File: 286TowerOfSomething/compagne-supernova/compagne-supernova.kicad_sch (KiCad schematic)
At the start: 3 parts, among them J1 Bus_ISA_16bit, U1 16550, U2 16550

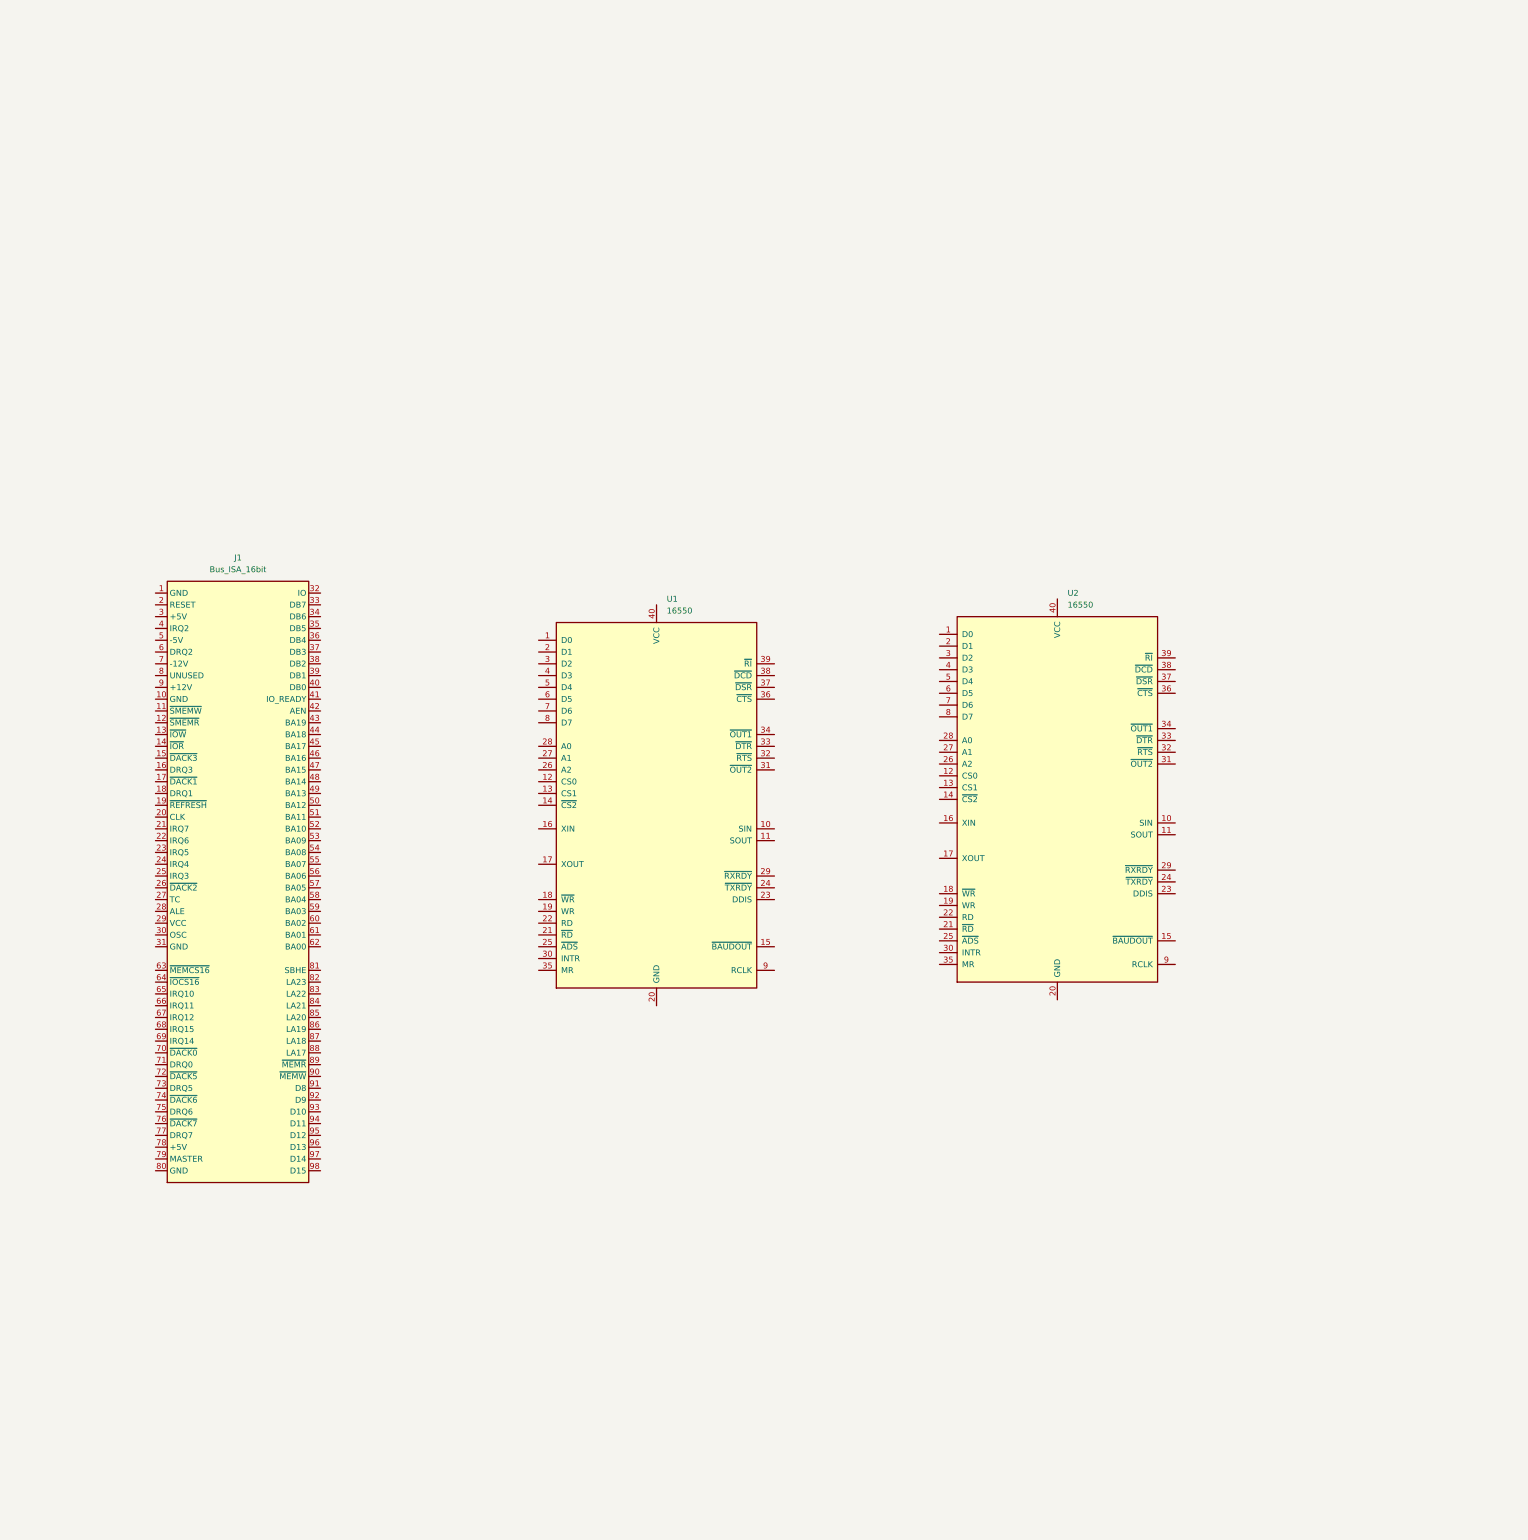
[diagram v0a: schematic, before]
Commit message: Schematic for compagne-supernova at like 50%
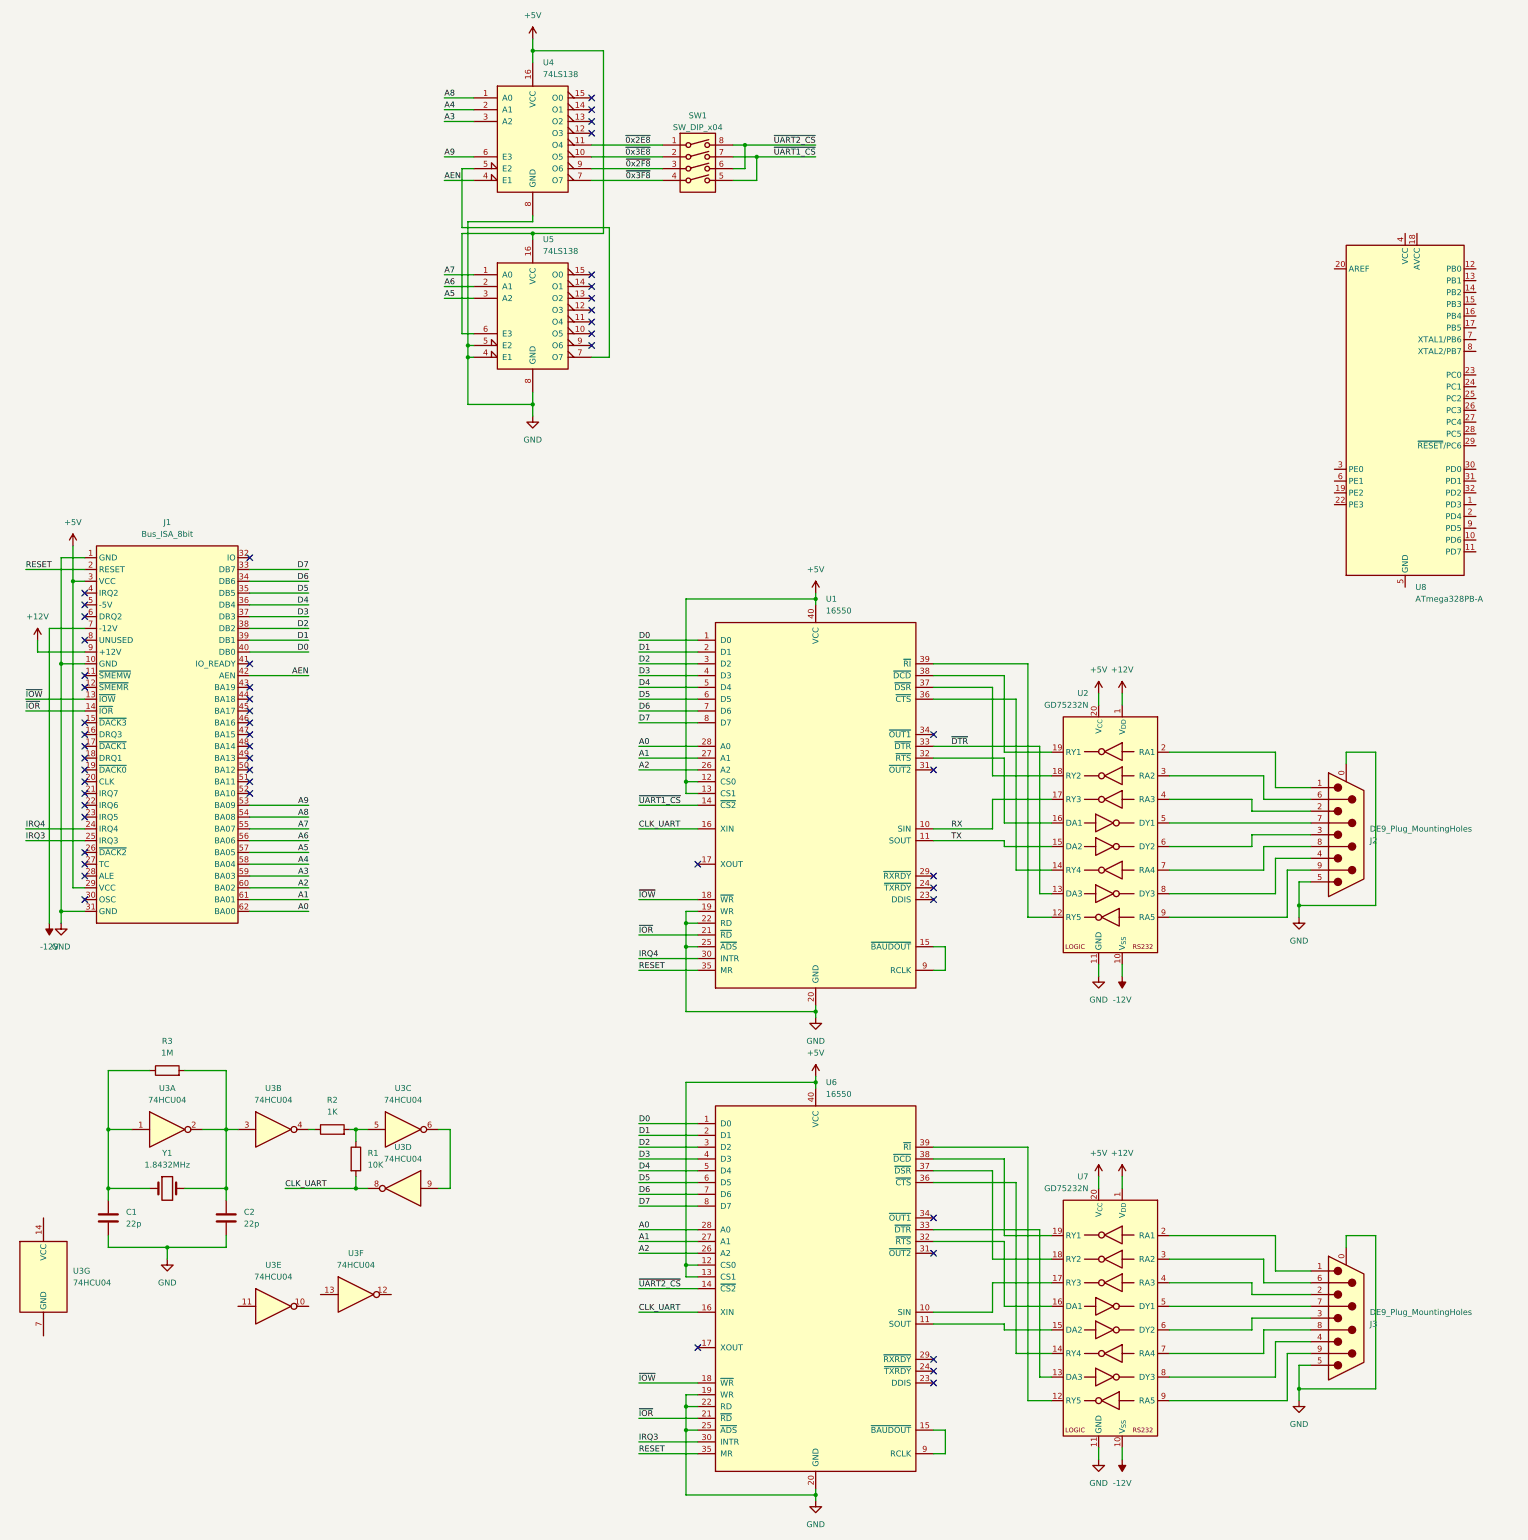
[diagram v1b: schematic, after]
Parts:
- removed J1: Bus_ISA_16bit, symbol Connector:Bus_ISA_16bit
- removed U2: 16550, Package_DIP:DIP-40_W15.24mm, symbol Interface_UART:16550
- added C1, C2: 22p, symbol Device:C
- added J1: Bus_ISA_8bit, symbol Connector:Bus_ISA_8bit
- added J2, J3: DE9_Plug_MountingHoles, symbol Connector:DE9_Plug_MountingHoles
- added R1: 10K, symbol Device:R
- added R2: 1K, symbol Device:R
- added R3: 1M, symbol Device:R
- added SW1: SW_DIP_x04, symbol Switch:SW_DIP_x04
- added U2, U7: GD75232N, Package_DIP:DIP-20_W7.62mm, symbol Interface_UART:GD75232N
- added U3: 74HCU04, symbol 74xx:74HC04
- added U4, U5: 74LS138, symbol 74xx:74LS138
- added U6: 16550, Package_DIP:DIP-40_W15.24mm, symbol Interface_UART:16550
- added U8: ATmega328PB-A, Package_QFP:TQFP-32_7x7mm_P0.8mm, symbol MCU_Microchip_ATmega:ATmega328PB-A
- added Y1: 1.8432MHz, symbol Device:Crystal
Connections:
- net D0: now reaches U1.1 (D0)
- net D0: now also J1.40 (DB0), U6.1 (D0)
- net RX: now reaches U1.10 (SIN)
- net RX: now also U2.17 (RY3)
- net TX: now reaches U1.11 (SOUT)
- net TX: now also U2.15 (DA2)
- net +5V: now reaches U1.12 (CS0)
- net +5V: now also U1.13 (CS1), U1.40 (VCC), J1.29 (VCC), J1.3 (VCC), U2.20 (V_{CC}), U4.16 (VCC), U5.16 (VCC), U5.6 (E3), U6.12 (CS0), U6.13 (CS1), U6.40 (VCC), U7.20 (V_{CC})
- net ~{UART1_CS}: now reaches U1.14 (~{CS2})
- net ~{UART1_CS}: now also SW1.5, SW1.7
- net at U1.15 (~{BAUDOUT}): now also U1.9 (RCLK)
- net CLK_UART: now reaches U1.16 (XIN)
- net CLK_UART: now also R1.2, U3.8, U6.16 (XIN)
- net ~{IOW}: now reaches U1.18 (~{WR})
- net ~{IOW}: now also J1.13 (~{IOW}), U6.18 (~{WR})
- net GND: now reaches U1.19 (WR)
- net GND: now also U1.20 (GND), U1.22 (RD), U1.25 (~{ADS}), C1.2, C2.2, J1.1 (GND), J1.10 (GND), J1.31 (GND), J2.0 (PAD), J2.5, J3.0 (PAD), J3.5, U2.11 (GND), U4.8 (GND), U5.4 (E1), U5.5 (E2), U5.8 (GND), U6.19 (WR), U6.20 (GND), U6.22 (RD), U6.25 (~{ADS}), U7.11 (GND)
- net D1: now reaches U1.2 (D1)
- net D1: now also J1.39 (DB1), U6.2 (D1)
- net ~{IOR}: now reaches U1.21 (~{RD})
- net ~{IOR}: now also J1.14 (~{IOR}), U6.21 (~{RD})
- net A2: now reaches U1.26 (A2)
- net A2: now also J1.60 (BA02), U6.26 (A2)
- net A1: now reaches U1.27 (A1)
- net A1: now also J1.61 (BA01), U6.27 (A1)
- net A0: now reaches U1.28 (A0)
- net A0: now also J1.62 (BA00), U6.28 (A0)
- net D2: now reaches U1.3 (D2)
- net D2: now also J1.38 (DB2), U6.3 (D2)
- net IRQ4: now reaches U1.30 (INTR)
- net IRQ4: now also J1.24 (IRQ4)
- net at U1.32 (~{RTS}): now also U2.16 (DA1)
- net ~{DTR}: now reaches U1.33 (~{DTR})
- net ~{DTR}: now also U2.13 (DA3)
- net RESET: now reaches U1.35 (MR)
- net RESET: now also J1.2 (RESET), U6.35 (MR)
- net at U1.36 (~{CTS}): now also U2.14 (RY4)
- net at U1.37 (~{DSR}): now also U2.18 (RY2)
- net at U1.38 (~{DCD}): now also U2.19 (RY1)
- net at U1.39 (~{RI}): now also U2.12 (RY5)
- net D3: now reaches U1.4 (D3)
- net D3: now also J1.37 (DB3), U6.4 (D3)
- net D4: now reaches U1.5 (D4)
- net D4: now also J1.36 (DB4), U6.5 (D4)
- net D5: now reaches U1.6 (D5)
- net D5: now also J1.35 (DB5), U6.6 (D5)
- net D6: now reaches U1.7 (D6)
- net D6: now also J1.34 (DB6), U6.7 (D6)
- net D7: now reaches U1.8 (D7)
- net D7: now also J1.33 (DB7), U6.8 (D7)
- new net: U8.21 (GND), U8.5 (GND)
- new net: U3.6, U3.9
- new net: R1.1, R2.2, U3.5
- new net: U4.5 (E2), U5.7 (O7)
- new net: C1.1, R3.1, U3.1, Y1.1
- new net: C2.1, R3.2, U3.2, U3.3, Y1.2
- new net: U6.39 (~{RI}), U7.12 (RY5)
- new net: U6.33 (~{DTR}), U7.13 (DA3)
- new net: U6.36 (~{CTS}), U7.14 (RY4)
- new net: U6.11 (SOUT), U7.15 (DA2)
- new net: U6.32 (~{RTS}), U7.16 (DA1)
- new net: U6.10 (SIN), U7.17 (RY3)
- new net: U6.37 (~{DSR}), U7.18 (RY2)
- new net: U6.38 (~{DCD}), U7.19 (RY1)
- new net: J3.1, U7.2 (RA1)
- new net: J3.6, U7.3 (RA2)
- new net: J3.2, U7.4 (RA3)
- new net: J3.7, U7.5 (DY1)
- new net: J3.3, U7.6 (DY2)
- new net: J3.8, U7.7 (RA4)
- new net: J3.4, U7.8 (DY3)
- new net: J3.9, U7.9 (RA5)
- new net: R2.1, U3.4
- new net: U6.15 (~{BAUDOUT}), U6.9 (RCLK)
- new net: J2.1, U2.2 (RA1)
- new net: J2.6, U2.3 (RA2)
- new net: J2.2, U2.4 (RA3)
- new net: J2.7, U2.5 (DY1)
- new net: J2.3, U2.6 (DY2)
- new net: J2.8, U2.7 (RA4)
- new net: J2.4, U2.8 (DY3)
- new net: J2.9, U2.9 (RA5)
- new net +12V: J1.9 (+12V), U2.1 (V_{DD}), U7.1 (V_{DD})
- new net -12V: J1.7 (-12V), U2.10 (V_{SS}), U7.10 (V_{SS})
- new net A3: J1.59 (BA03), U4.3 (A2)
- new net A4: J1.58 (BA04), U4.2 (A1)
- new net A5: J1.57 (BA05), U5.3 (A2)
- new net A6: J1.56 (BA06), U5.2 (A1)
- new net A7: J1.55 (BA07), U5.1 (A0)
- new net A8: J1.54 (BA08), U4.1 (A0)
- new net A9: J1.53 (BA09), U4.6 (E3)
- new net AEN: J1.42 (AEN), U4.4 (E1)
- new net IRQ3: J1.25 (IRQ3), U6.30 (INTR)
- new net ~{0x2E8}: SW1.1, U4.11 (O4)
- new net ~{0x2F8}: SW1.3, U4.9 (O6)
- new net ~{0x3E8}: SW1.2, U4.10 (O5)
- new net ~{0x3F8}: SW1.4, U4.7 (O7)
- new net ~{UART2_CS}: SW1.6, SW1.8, U6.14 (~{CS2})
- no-connect marks 0 -> 54
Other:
- moved on the sheet: U1

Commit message: Finished schematic of compagne-supernova. Started messing with layout.
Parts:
- removed U8: ATmega328PB-A, Package_QFP:TQFP-32_7x7mm_P0.8mm, symbol MCU_Microchip_ATmega:ATmega328PB-A
- added C10, C12, C13, C15, C16, C3, C4, C5, C6, C7, C9: 100n, Capacitor_SMD:C_0603_1608Metric_Pad1.08x0.95mm_HandSolder, symbol Device:C
- added C11, C14, C8: 22u, Capacitor_SMD:CP_Elec_5x5.3, symbol Device:C_Polarized
- C1, C2: footprint (none) -> Capacitor_SMD:C_0603_1608Metric_Pad1.08x0.95mm_HandSolder
- J1: footprint (none) -> pc-parts:BUS_AT_8BIT
- J2, J3: value DE9_Plug_MountingHoles -> DE9; footprint (none) -> Connector_Dsub:DSUB-9_Male_Horizontal_P2.77x2.84mm_EdgePinOffset7.70mm_Housed_MountingHolesOffset9.12mm
- R1, R2, R3: footprint (none) -> Resistor_SMD:R_0603_1608Metric_Pad0.98x0.95mm_HandSolder
- SW1: footprint (none) -> Button_Switch_THT:SW_DIP_SPSTx04_Slide_9.78x12.34mm_W7.62mm_P2.54mm
- U3: footprint (none) -> Package_SO:SO-14_3.9x8.65mm_P1.27mm
- U4, U5: footprint (none) -> Package_DIP:DIP-16_W7.62mm
- Y1: footprint (none) -> Crystal:Crystal_HC49-U_Vertical
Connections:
- net +12V: now also C11.1, C12.1, C13.1
- net +5V: now also U3.14 (VCC), C10.1, C3.1, C4.1, C5.1, C6.1, C7.1, C8.1, C9.1
- net -12V: now also C14.2, C15.2, C16.2
- net GND: now also U3.13, U3.5, U3.7 (GND), C10.2, C11.2, C12.2, C13.2, C14.1, C15.1, C16.1, C3.2, C4.2, C5.2, C6.2, C7.2, C8.2, C9.2
- net at U3.9: now also U3.10; no longer U3.6
- net at R1.1, R2.2: now also U3.11; no longer U3.5
- net ~{RTS}: now reaches U1.32 (~{RTS}), U2.16 (DA1)
- net TX: no longer names the net of U1.11 (SOUT), U2.15 (DA2)
- net ~{DTR}: no longer names the net of U1.33 (~{DTR}), U2.13 (DA3)
- no-connect marks 54 -> 57
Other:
- added sheet PS2 to Serial (ps2_to_serial.kicad_sch)
- company: (none) -> Surreality Labs
- title: (none) -> COMpagne Supernova
- moved on the sheet: C1, C2, J1, J2, J3, R1, R2, R3, SW1, U1, U2, U3A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

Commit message: Doing some work on the compagne-supernova layout
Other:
- sheet PS2 to Serial ports: added RX, ~{RTS}; removed none
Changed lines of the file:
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@@
 	(wire
 		(pts
+			(xy 295.91 24.13) (xy 307.34 24.13)
+		)
+		(stroke
+			(width 0)
+			(type default)
+		)
+	)
+	(wire
+		(pts
 			(xy 134.62 72.39) (xy 134.62 74.93)
 		)
@@
 	(wire
 		(pts
+			(xy 295.91 21.59) (xy 307.34 21.59)
+		)
+		(stroke
+			(width 0)
+			(type default)
+		)
+	)
+	(wire
+		(pts
 			(xy 142.24 90.17) (xy 142.24 80.01)
 		)
@@
 		)
 	)
+	(label "RX"
+		(at 295.91 21.59 0)
+		(fields_autoplaced yes)
+		(effects
+			(font
+				(size 1.27 1.27)
+			)
+			(justify left bottom)
+		)
+	)
 	(label "A3"
 		(at 120.65 186.69 180)
@@
 		)
 	)
+	(label "~{RTS}"
+		(at 295.91 24.13 0)
+		(fields_autoplaced yes)
+		(effects
+			(font
+				(size 1.27 1.27)
+			)
+			(justify left bottom)
+		)
+	)
 	(label "CLK_UART"
 		(at 260.35 148.59 0)
@@
 			)
 		)
+		(pin "RX" input
+			(at 307.34 21.59 180)
+			(effects
+				(font
+					(size 1.27 1.27)
+				)
+				(justify left)
+			)
+		)
+		(pin "~{RTS}" input
+			(at 307.34 24.13 180)
+			(effects
+				(font
+					(size 1.27 1.27)
+				)
+				(justify left)
+			)
+		)
